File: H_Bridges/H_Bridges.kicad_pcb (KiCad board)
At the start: 4 copper layers, 112.4 x 81.7 mm, 64 parts, among them J1 S4B-PH-K-SLFSN, J2 USB4085-GF-A_REVB, Q1 IRF540NSTRLPBF, Q10 PMOS, Q2 IRF540NSTRLPBF, Q3 IRF540NSTRLPBF, Q4 IRF540NSTRLPBF, Q5 IRF540NSTRLPBF, Q6 IRF540NSTRLPBF, Q7 IRF540NSTRLPBF, Q8 IRF540NSTRLPBF, Q9 PMOS, U1 ESP8266, U2 max1898eub42+T, U3 TPS61023DRLR

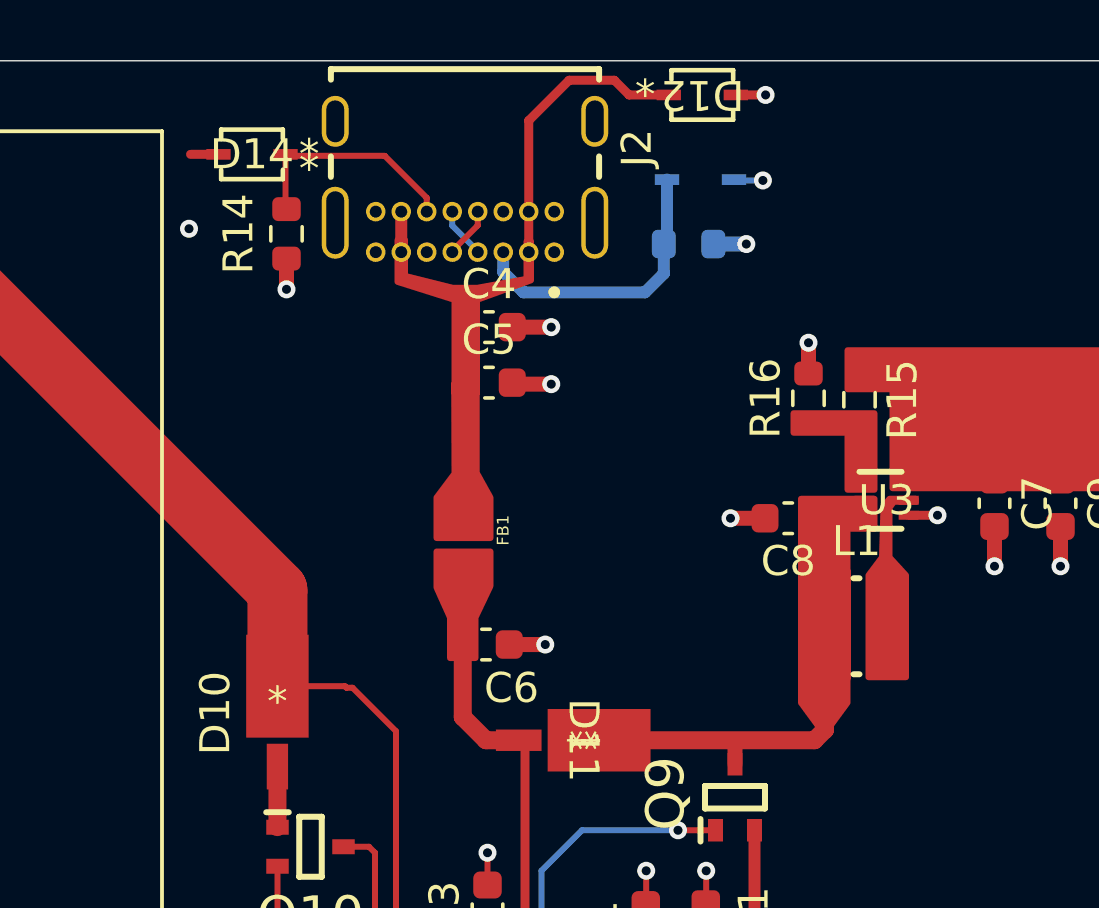
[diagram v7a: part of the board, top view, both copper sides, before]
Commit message: updated inductor footprint
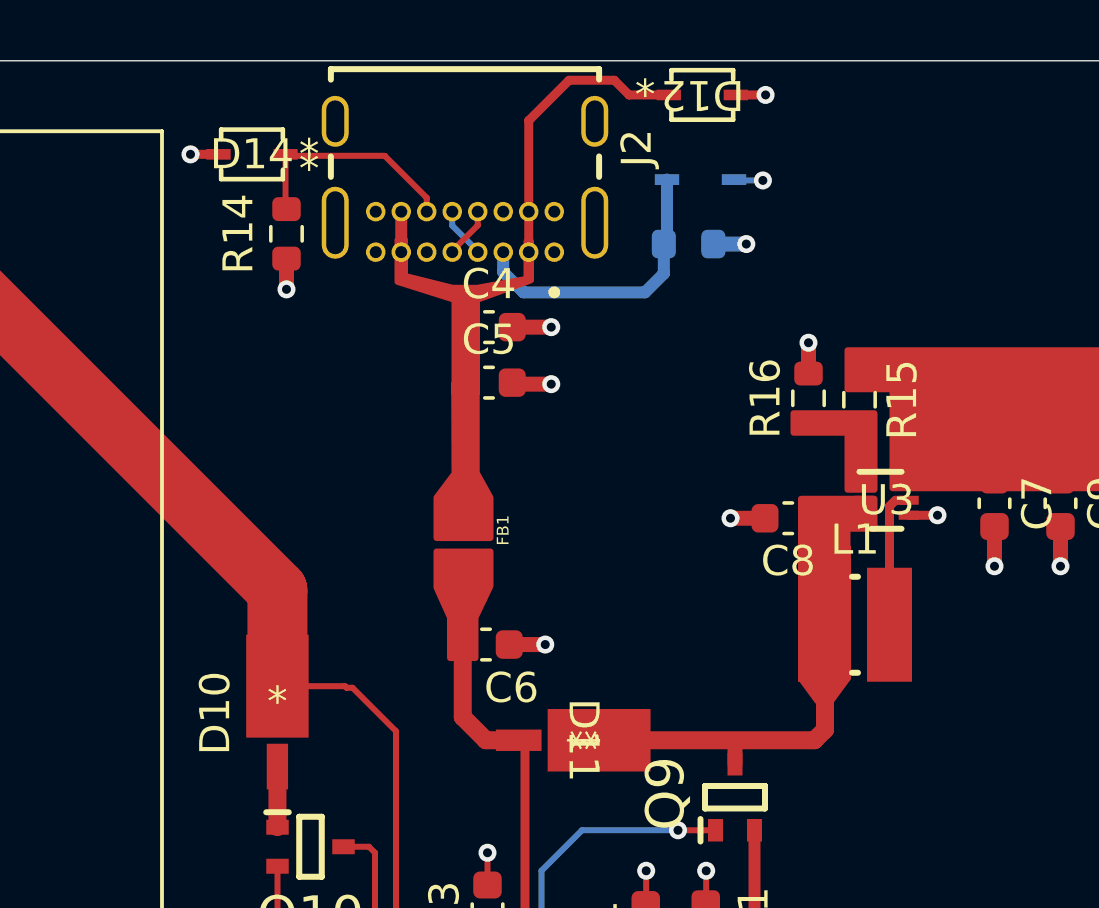
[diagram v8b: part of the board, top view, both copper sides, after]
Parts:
- moved L1 0.07 mm to (135.2, 65.6)
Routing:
- net Net-(U3-SW): track 0.00 -> 4.67 mm
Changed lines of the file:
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@@
 		(at 187.199908 114.349802 90)
 		(property "Reference" "G***"
-			(at 0 0 270)
+			(at 0 0 -90)
 			(layer "F.SilkS")
 			(hide yes)
@@
 		)
 		(property "Value" "LOGO"
-			(at 0.75 0 270)
+			(at 0.75 0 -90)
 			(layer "F.SilkS")
 			(hide yes)
@@
 		(at 124.89 111.583 90)
 		(property "Reference" "U4"
-			(at -7.225 -11.235 270)
+			(at -7.225 -11.235 -90)
 			(layer "F.SilkS")
 			(effects
@@
 		)
 		(property "Value" "~"
-			(at -1.51 11.065 270)
+			(at -1.51 11.065 -90)
 			(layer "F.Fab")
 			(effects
@@
 	(footprint "Footprints:WE-MAPI_3015"
 		(layer "F.Cu")
-		(at 135.3 65.65)
+		(at 135.25 65.6)
 		(descr "<b>WE-MAPI  SMD Power Inductorr<br></b><br>Size:3015,SMT,2pins<br>LXWXH=3X3X1.5mm")
 		(property "Reference" "L1"
@@
 			)
 		)
-		(sheetname "Charger")
-		(sheetfile "chargecircuit.kicad_sch")
 		(attr smd)
 		(fp_line
@@
 		(fp_poly
 			(pts
-				(xy -1.9 -1.9) (xy 1.9 -1.9) (xy 1.9 1.9) (xy -1.9 1.9)
+				(xy -1.9508 -1.9508) (xy 1.9762 -1.9508) (xy 1.9762 1.9508) (xy -1.9508 1.9508)
 			)
 			(stroke
@@
 		)
 		(pad "1" smd rect
-			(at -1.05 0)
-			(size 1.3 3.4)
+			(at -1.15 0)
+			(size 1.5 3.8)
 			(layers "F.Cu" "F.Paste" "F.Mask")
 			(net 8 "VCC")
@@
 		)
 		(pad "2" smd rect
-			(at 1.05 0)
-			(size 1.3 3.4)
+			(at 1.15 0)
+			(size 1.5 3.8)
 			(layers "F.Cu" "F.Paste" "F.Mask")
 			(net 21 "Net-(U3-SW)")
@@
 			(polygon
 				(pts
-					(xy 134.9 63.95) (xy 135.7 63.95) (xy 135.7 67.35) (xy 134.9 67.35)
+					(xy 134.85 63.9) (xy 135.65 63.9) (xy 135.65 67.3) (xy 134.85 67.3)
 				)
 			)
@@
 			(polygon
 				(pts
-					(xy 134.9 63.95) (xy 135.7 63.95) (xy 135.7 67.35) (xy 134.9 67.35)
+					(xy 134.85 63.9) (xy 135.65 63.9) (xy 135.65 67.3) (xy 134.85 67.3)
 				)
 			)
@@
 	(gr_poly
 		(pts
-			(xy 137.28 61.5) (xy 137.28 61.4) (xy 136.4 61.4) (xy 136.2 61.65) (xy 136.15 63.35) (xy 135.7 63.95)
-			(xy 135.7 67.35) (xy 136.95 67.35) (xy 136.95 63.95) (xy 136.4 63.35) (xy 136.4 61.7) (xy 136.55 61.5)
-		)
-		(stroke
-			(width 0.2)
-			(type solid)
-		)
-		(fill solid)
-		(layer "F.Cu")
-		(net 21)
-	)
-	(gr_poly
-		(pts
 			(xy 121.3 63.16) (xy 121.3 64.36) (xy 121.75 65.36) (xy 121.75 66.71) (xy 122.6 66.71) (xy 122.6 65.36)
 			(xy 123.1 64.31) (xy 123.1 63.16)
@@
 	(gr_poly
 		(pts
-			(xy 134 68.95) (xy 133.45 68.2) (xy 133.45 63.8) (xy 135 63.8) (xy 135 68.2) (xy 134.45 68.95)
+			(xy 134 68.15) (xy 133.45 67.4) (xy 133.45 63) (xy 135 63) (xy 135 67.4) (xy 134.45 68.15)
 		)
 		(stroke
@@
 	)
 	(via blind
-		(at 113.05 52.4)
+		(at 113.1 49.92)
 		(size 0.6)
 		(drill 0.3)
@@
 	)
 	(segment
+		(start 136.4 65.6)
+		(end 136.4 61.65)
+		(width 0.3)
+		(layer "F.Cu")
+		(net 21)
+	)
+	(segment
+		(start 136.4 61.65)
+		(end 136.599169 61.450831)
+		(width 0.3)
+		(layer "F.Cu")
+		(net 21)
+	)
+	(segment
+		(start 136.599169 61.450831)
+		(end 137.040001 61.450831)
+		(width 0.3)
+		(layer "F.Cu")
+		(net 21)
+	)
+	(segment
